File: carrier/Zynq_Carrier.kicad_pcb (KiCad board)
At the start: 4 copper layers, 148 x 137 mm, 533 parts, among them J11001 Header_2x20_2.54mm, J12001 HDMI-019S, J14001 HDMI-019S, J15001 AFC07-S40FCA-00, J16001 TF-01A, J17001 TYPE-C-31-M-12, J18001 DS1024-2x6R2, J18002 DS1024-2x6R2, J19001 DS1024-2x6R2, J2001 ZX-SH1.0-4PWT, J23001 KH-5224-8P8C-D, J24001 DF40C-100DS-0.4V(51), J25002 DF40C-100DS-0.4V(51), J26003 DF40C-100DS-0.4V(51), J29001 TYPE-C-31-M-12, J31001 TYPE-C-31-M-12, J32002 TYPE-C-31-M-12, J8001 SFW15R-1STE1LF, J9001 878311420, J9002 HX_JN1.27-2x5, Q20001 AO3400A, SW1001 DSHP04TSGER, SW19001 DSHP04TSGER, SW28001 DSHP04TSGER, SW33001 USER, SW33002 USER, SW33003 USER, SW33004 USER, SW7001 DSHP04TSGER, SW7002 DSHP08TSGER, SW7003 TS-1187A-B-A-B, SW7004 TS-1187A-B-A-B, SW7005 TS-1187A-B-A-B, SW7006 DSHP04TSGER, SW9001 DIP-4, SW9002 RESET, T10001 HX5008NLT, U1001 SY6280AAC, U1002 PCA9306DCUR, U11001 TLV75725PDYDR, U12001 M24C02-WMN6TP, U12002 TPD4E02B04DQAR, U12003 TPD4E02B04DQAR, U12004 TPD4E05U06DQAR, U14001 TPD12S016PWR, U15001 SY7201ABC, U15002 USBLC6-2SC6, U16001 TXS02612RTWR, U16002 TPD6E001RSER, U17001 TPS26631PWPR, U17002 USBLC6-2SC6, U19001 SY6280AAC, U19002 TPD4E1U06, U19003 TPD4E1U06, U20001 LM61460AANRJRR, U20002 LM61460AANRJRR, U20003 AP2112K-1.8, U2001 USBLC6-2SC6, U21001 INA3221AIRGVR, U21002 INA3221AIRGVR, U22004 LM61460AANRJRR, U27001 CP2102N-A02, U28001 CH347T, U28002 SN74LVC125ADR, U28004 AP2112K-3.3TRG1, U29001 USBLC6-2SC6, U30001 FUSB302BMPX, U3001 24AA025E48T-I/OT, U3002 RV-3028-C7-32.768kHz-1ppm-TA-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, U3003 TPS3823-33DBVR, U31001 USBLC6-2SC6, U32001 TPS2051CDBVR, U32002 USBLC6-2SC6, U4001 SN74LVC1G08, U4002 SN74LVC1G08, U4003 SN74LVC1G08, U5001 SN74LVC1G08, U5002 SN74LVC1G08, U5003 SN74LVC1G08, U5004 SN74LVC1G08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

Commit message: fix: USB-C mated INWARD — correct BOTH footprint mating-face AND 3D model + the gate
User caught (at an ANGLE — top-down hid it) that all 4 USB-C (J17001/J29001/J31001/
J32002) opened their cavity INBOARD. A full ultracode 2D-vs-3D angle audit of every
component confirmed the USB-C is the ONLY mismatch class; all other connectors +
components are correct. Two real defects, both fixed:

1. FOOTPRINT mating face: CONN_MATING_FACE["TYPE-C-31-M-12"] "-Y" -> "+Y". The 12 SMD
   signal contacts are the dense row at local -Y, so the mouth is OPPOSITE = +Y. With
   "-Y" the placer left the pads' mouth facing inboard on the N edge; "+Y" places the
   4 USB-C at rot 180 with the pad mouth toward the edge.
2. 3D MODEL: the EasyEDA .wrl was authored with its cavity 180 deg from its own
   footprint (cavity at the SMT-tail side). parts/TYPE-C-31-M-12/TYPE-C-31-M-12.kicad_mod
   model (rotate (xyz 0 0 0)) -> (xyz 0 0 180) aligns the model cavity with the
   footprint mouth; offset unchanged. ANGLED render confirms the cavity now faces
   off-board for all 4.

GATE fixes (LAW 4 — it MISSED this; make it correct, not softer):
 * connector_model_gate._tail_row_mouth: derive the tail row from EVERY pad (was
   _NUMERIC-only, which matched only the 4 shell legs and missed the 12 signal
   contacts named B8/A5/... — so it spuriously "agreed" with the wrong -Y). Now the
   densest y-row is the real contact row; mouth opposite -> correctly derives +Y.
 * bad-Z check: model rotate Z must be 0 OR 180 (axis-aligned; 180 = valid in-plane
   mouth flip for a .wrl authored on the opposite end). Was "0 mod 360" — a
   misdiagnosis that BOTH forbade the corrective 180 and gave false confidence to a
   .wrl mis-authored at 0. 90/270 (perpendicular) and non-orthogonal still fail.
   The model OPENING direction remains the render's job (LAW 5/6) — the gate can't render.

Verified: 148x137, DRC 0, all LAW-5/6 gates PASS (0 bad-Z, 0 geom-conflict), 3D MODELS
55/55, 633 tests pass, USB-C cavities rend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
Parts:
- moved J17001 0.25 mm to (91.8, 28.8), turned to 180 degrees
- moved J29001 0.25 mm to (129.9, 28.8), turned to 180 degrees
- moved J31001 0.25 mm to (141.4, 28.8), turned to 180 degrees
- moved J32002 0.25 mm to (114.7, 28.8), turned to 180 degrees

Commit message: feat: short FUNCTION descriptor on silk beside every off-board connector
User: "very short descriptors for each connector so we know which connector is for
what." Added a programmatic top-silk label per off-board connector, derived from its
subsystem sheet (never hand-placed):
  PWR (USB-C PD in) · USB OTG · JTAG · UART · microSD · HDMI TX · HDMI RX · ETH ·
  QWIIC · CAM · LCD · PMOD0/1/2
placed just inboard of the connector courtyard, centred on its along-edge axis.

The connector's J-ref is HIDDEN on silk (the function label owns the clear spot — the
ref was the space competitor; it stays in the footprint data for the netlist/BOM).
This is the dev-board idiom: label connectors by FUNCTION, not "J17001".

Implementation (schgen/generate/pcb.py): _CONN_DESC (sheet->label) + the PMODs
numbered in ref order; _connector_descriptors() emits the gr_text labels (F.SilkS,
size 1.1) and emit_pcb appends them; _embed_footprint hides the Reference property
for CONN_MATING_FACE parts. Verified silk-only AND 3D render per edge — all 14 labels
read cleanly, no overlap (the earlier "clutter" was the non-printed F.Fab layer).

Verified: 148x137, DRC 0, BOARD PASS, all gates green, 636 tests pass (+3 new
descriptor tests: all functions present, on-board F.SilkS, connector refs hidden /
IC refs kept).

Co-Authored-By: Claude Opus 4.8 <noreply@anthropic.com>
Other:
- board text added: "CAM"
- board text added: "ETH"
- board text added: "HDMI RX"
- board text added: "HDMI TX"
- board text added: "JTAG"
- board text added: "LCD"
- board text added: "PMOD0"
- board text added: "PMOD1"
- board text added: "PMOD2"
- board text added: "PWR"
- board text added: "QWIIC"
- board text added: "UART"
- board text added: "USB OTG"
- board text added: "microSD"
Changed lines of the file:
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@@
 			"Reference"
 			"J12001"
+			(hide yes)
 			(at 0 -5.42 0)
 			(layer "F.SilkS")
@@
 			"Reference"
 			"J14001"
+			(hide yes)
 			(at 0 -5.42 0)
 			(layer "F.SilkS")
@@
 			"Reference"
 			"J15001"
+			(hide yes)
 			(at 0 -3.44 0)
 			(layer "F.SilkS")
@@
 			"Reference"
 			"J16001"
+			(hide yes)
 			(at 0 -7.28 0)
 			(layer "F.SilkS")
@@
 			"Reference"
 			"J17001"
+			(hide yes)
 			(at 0 -4.47 0)
 			(layer "F.SilkS")
@@
 			"Reference"
 			"J18001"
+			(hide yes)
 			(at 0 -3.27 0)
 			(layer "F.SilkS")
@@
 			"Reference"
 			"J18002"
+			(hide yes)
 			(at 0 -3.27 0)
 			(layer "F.SilkS")
@@
 			"Reference"
 			"J19001"
+			(hide yes)
 			(at 0 -3.27 0)
 			(layer "F.SilkS")
@@
 			"Reference"
 			"J2001"
+			(hide yes)
 			(at 0 -3.7 0)
 			(layer "F.SilkS")
@@
 			"Reference"
 			"J23001"
+			(hide yes)
 			(at 0 -8.5 0)
 			(layer "F.SilkS")
@@
 			"Reference"
 			"J29001"
+			(hide yes)
 			(at 0 -4.47 0)
 			(layer "F.SilkS")
@@
 			"Reference"
 			"J31001"
+			(hide yes)
 			(at 0 -4.47 0)
 			(layer "F.SilkS")
@@
 			"Reference"
 			"J32002"
+			(hide yes)
 			(at 0 -4.47 0)
 			(layer "F.SilkS")
@@
 			"Reference"
 			"J8001"
+			(hide yes)
 			(at 0 -3.05 0)
 			(layer "F.SilkS")
@@
 			)
 		)
+	)
+	(gr_text
+		"HDMI RX"
+		(at 44.11 150.8 0)
+		(layer "F.SilkS")
+		(effects
+			(font
+				(size 1.1 1.1)
+				(thickness 0.2)
+			)
+		)
+	)
+	(gr_text
+		"HDMI TX"
+		(at 80.94 150.8 0)
+		(layer "F.SilkS")
+		(effects
+			(font
+				(size 1.1 1.1)
+				(thickness 0.2)
+			)
+		)
+	)
+	(gr_text
+		"LCD"
+		(at 32.336 100.98 0)
+		(layer "F.SilkS")
+		(effects
+			(font
+				(size 1.1 1.1)
+				(thickness 0.2)
+			)
+		)
+	)
+	(gr_text
+		"microSD"
+		(at 74.95 39.402 0)
+		(layer "F.SilkS")
+		(effects
+			(font
+				(size 1.1 1.1)
+				(thickness 0.2)
+			)
+		)
+	)
+	(gr_text
+		"PWR"
+		(at 91.835 33.698 0)
+		(layer "F.SilkS")
+		(effects
+			(font
+				(size 1.1 1.1)
+				(thickness 0.2)
+			)
+		)
+	)
+	(gr_text
+		"PMOD0"
+		(at 121.45 155.482 0)
+		(layer "F.SilkS")
+		(effects
+			(font
+				(size 1.1 1.1)
+				(thickness 0.2)
+			)
+		)
+	)
+	(gr_text
+		"PMOD1"
+		(at 138.19 155.482 0)
+		(layer "F.SilkS")
+		(effects
+			(font
+				(size 1.1 1.1)
+				(thickness 0.2)
+			)
+		)
+	)
+	(gr_text
+		"PMOD2"
+		(at 155.74 155.482 0)
+		(layer "F.SilkS")
+		(effects
+			(font
+				(size 1.1 1.1)
+				(thickness 0.2)
+			)
+		)
+	)
+	(gr_text
+		"QWIIC"
+		(at 165.3 100.27 0)
+		(layer "F.SilkS")
+		(effects
+			(font
+				(size 1.1 1.1)
+				(thickness 0.2)
+			)
+		)
+	)
+	(gr_text
+		"ETH"
+		(at 155.7 87.17 0)
+		(layer "F.SilkS")
+		(effects
+			(font
+				(size 1.1 1.1)
+				(thickness 0.2)
+			)
+		)
+	)
+	(gr_text
+		"JTAG"
+		(at 129.935 33.698 0)
+		(layer "F.SilkS")
+		(effects
+			(font
+				(size 1.1 1.1)
+				(thickness 0.2)
+			)
+		)
+	)
+	(gr_text
+		"UART"
+		(at 141.365 33.698 0)
+		(layer "F.SilkS")
+		(effects
+			(font
+				(size 1.1 1.1)
+				(thickness 0.2)
+			)
+		)
+	)
+	(gr_text
+		"USB OTG"
+		(at 114.695 33.698 0)
+		(layer "F.SilkS")
+		(effects
+			(font
+				(size 1.1 1.1)
+				(thickness 0.2)
+			)
+		)
+	)
+	(gr_text
+		"CAM"
+		(at 32.4 75.72 0)
+		(layer "F.SilkS")
+		(effects
+			(font
+				(size 1.1 1.1)
+				(thickness 0.2)
+			)
+		)

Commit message: feat: silk descriptors for the interior headers too (GPIO / JTAG / SWD)
Extend the self-documenting silk labels to the on-board developer headers (user:
"each connector"): J11001 -> GPIO (FMC-site 2x20 breakout), J9001 -> JTAG (Zynq 2x7
2.00mm header), J9002 -> SWD (system-controller ARM 10-pin). Labels placed below
each header; their J-refs hidden like the off-board connectors. The SoM DF40
mezzanines are intentionally NOT labelled — the "Zynq SoM" body silk already marks
that region (the module mounts on them).

_INT_DESC (ref->label) added at module level; _embed_footprint hides the ref for
CONN_MATING_FACE OR _INT_DESC; _connector_descriptors emits the interior labels.
Render-verified (silk-only): GPIO/JTAG/SWD readable beside their headers.

Verified: 148x137, DRC 0, BOARD PASS, all gates; descriptor tests updated
(GPIO/SWD present, interior count, J11001 ref hidden).

Co-Authored-By: Claude Opus 4.8 <noreply@anthropic.com>
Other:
- board text added: "GPIO"
- board text added: "SWD"
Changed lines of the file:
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@@
 			"Reference"
 			"J11001"
+			(hide yes)
 			(at 1.27 -2.38 0)
 			(layer "F.SilkS")
@@
 			"Reference"
 			"J9001"
+			(hide yes)
 			(at 0 -3 0)
 			(layer "F.SilkS")
@@
 			"Reference"
 			"J9002"
+			(hide yes)
 			(at 0 -4.02 0)
 			(layer "F.SilkS")
@@
 		(layer "F.SilkS")
 		(effects
+			(font
+				(size 1.1 1.1)
+				(thickness 0.2)
+			)
+		)
+	)
+	(gr_text
+		"GPIO"
+		(at 98.845 71.15 0)
+		(layer "F.SilkS")
+		(effects
+			(font
+				(size 1.1 1.1)
+				(thickness 0.2)
+			)
+		)
+	)
+	(gr_text
+		"JTAG"
+		(at 102.855 142.234 0)
+		(layer "F.SilkS")
+		(effects
+			(font
+				(size 1.1 1.1)
+				(thickness 0.2)
+			)
+		)
+	)
+	(gr_text
+		"SWD"
+		(at 100.88 135.434 0)
+		(layer "F.SilkS")
+		(effects

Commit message: fix: 3 CRITICAL electrical defects from the multi-agent audit (SW2 / LCD D1 / JTAG TDI-TDO)
A 69-agent electrical audit (35 per-subsystem + 7 cross-cutting, every finding
adversarially refuted) surfaced 3 board-dead CRITICAL defects that passed DRC/ERC/
netlist-equivalence. Each independently re-verified from the source artifacts before
fixing (per the "audits over-confirm; fixes can introduce bugs" rule):

1. SW2 (DSHP08) module DIP shorted all enables. Each DIP rocker bridges the two
   pads in the SAME COLUMN; the DSHP08 footprint numbers its bottom row 9..16
   (UNLIKE DSHP04's 8..5), so positions pair (n, n+8) — but the adapter re-used
   DSHP04's (n,17-n) diagonal, shorting +3V3_SC to itself on 1/3/5/7 and tying two
   enable nets on 2/4/6/8. All 7 module enables stuck off. FIX in the ADAPTER
   (+3V3_SC on top pins 1-8, BU_DIP nets on bottom pins 9-16) — NOT by renumbering
   the faithful EasyEDA footprint as the audit suggested (that would corrupt the
   real-part mapping; "never redraw parts"). DSHP08 is used only by SW2.
   + footprint-aware regression test (reads same-column pairs, asserts each rocker
     bridges +3V3_SC -> one unique BU_DIP enable) for SW2 and SW1.

2. LCD SY7201 boost catch diode D1 (SS34) reversed — cathode on LX, anode on the
   output, so the boost could never pump VLED+ (dead backlight). Device:D_Schottky
   is pin1=K/pin2=A; put K (D1.1) on the output, A (D1.2) on LX. The dossier was
   already correct; the netlist contradicted it.

3. usb_jtag CH347T TDI/TDO swapped — pin7=RTS0/MISO/TDO (bridge input), pin8=
   TXD0/MOSI/TDI (bridge output). DBG_FT_TDI sat on the input pin (buffer 2A had
   no driver) and DBG_FT_TDO on the output pin (collides with buffer 3Y when the
   bridge enables). Swapped to U1.8/U1.7; doc table corrected.

Verified: 148x137, DRC 0, netlist-equivalence PASS on all 35 sheets, every LAW gate
green, 68 subsystem tests pass.

Co-Authored-By: Claude Opus 4.8 <noreply@anthropic.com>
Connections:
- D15001 pad 1: Net-(D15001-K) -> /lcd/LCD_VLED_P
- D15001 pad 2: /lcd/LCD_VLED_P -> Net-(D15001-A)
- L15001 pad 2: Net-(D15001-K) -> Net-(D15001-A)
- SW7002 pad 10: BU_DIP_PMOD -> BU_DIP_HDMI_RX
- SW7002 pad 11: +3V3_SC -> BU_DIP_LCD
- SW7002 pad 12: BU_DIP_SD -> BU_DIP_CAM
- SW7002 pad 13: +3V3_SC -> BU_DIP_SD
- SW7002 pad 14: BU_DIP_LCD -> BU_DIP_USB
- SW7002 pad 15: +3V3_SC -> BU_DIP_PMOD
- SW7002 pad 16: BU_DIP_HDMI_TX -> BU_DIP_SPARE
- SW7002 pad 2: BU_DIP_HDMI_RX -> +3V3_SC
- SW7002 pad 4: BU_DIP_CAM -> +3V3_SC
- SW7002 pad 6: BU_DIP_USB -> +3V3_SC
- SW7002 pad 8: BU_DIP_SPARE -> +3V3_SC
- SW7002 pad 9: +3V3_SC -> BU_DIP_HDMI_TX
- U15001 pad 1: Net-(D15001-K) -> Net-(D15001-A)
- U28001 pad 7: /usb_jtag/DBG_FT_TDI -> /usb_jtag/DBG_FT_TDO
- U28001 pad 8: /usb_jtag/DBG_FT_TDO -> /usb_jtag/DBG_FT_TDI
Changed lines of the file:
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@@
 	(net 271 "Net-(C22021-Pad2)")
 	(net 272 "Net-(D1001-K)")
-	(net 273 "Net-(D15001-K)")
+	(net 273 "Net-(D15001-A)")
 	(net 274 "Net-(D19001-K)")
 	(net 275 "Net-(D20001-K)")
@@
 			(layers "F.Cu" "F.Mask" "F.Paste")
 			(roundrect_rratio 0.138889)
-			(net 273 "Net-(D15001-K)")
+			(net 47 "/lcd/LCD_VLED_P")
 		)
 		(pad
@@
 			(layers "F.Cu" "F.Mask" "F.Paste")
 			(roundrect_rratio 0.138889)
-			(net 47 "/lcd/LCD_VLED_P")
+			(net 273 "Net-(D15001-A)")
 		)
 		(embedded_fonts no)
@@
 			(size 1.599997 3.499993)
 			(layers "F.Cu" "F.Paste" "F.Mask")
-			(net 273 "Net-(D15001-K)")
+			(net 273 "Net-(D15001-A)")
 		)
 		(pad
@@
 			(size 0.759993 1.599997)
 			(layers "F.Cu" "F.Paste" "F.Mask")
-			(net 84 "BU_DIP_HDMI_RX")
+			(net 14 "+3V3_SC")
 		)
 		(pad
@@
 			(size 0.759993 1.599997)
 			(layers "F.Cu" "F.Paste" "F.Mask")
-			(net 83 "BU_DIP_CAM")
+			(net 14 "+3V3_SC")
 		)
 		(pad
@@
 			(size 0.759993 1.599997)
 			(layers "F.Cu" "F.Paste" "F.Mask")
-			(net 92 "BU_DIP_USB")
+			(net 14 "+3V3_SC")
 		)
 		(pad
@@
 			(size 0.759993 1.599997)
 			(layers "F.Cu" "F.Paste" "F.Mask")
-			(net 91 "BU_DIP_SPARE")
+			(net 14 "+3V3_SC")
 		)
 		(pad
@@
 			(size 0.759993 1.599997)
 			(layers "F.Cu" "F.Paste" "F.Mask")
-			(net 14 "+3V3_SC")
+			(net 85 "BU_DIP_HDMI_TX")
 		)
 		(pad
@@
 			(size 0.759993 1.599997)
 			(layers "F.Cu" "F.Paste" "F.Mask")
-			(net 89 "BU_DIP_PMOD")
+			(net 84 "BU_DIP_HDMI_RX")
 		)
 		(pad
@@
 			(size 0.759993 1.599997)
 			(layers "F.Cu" "F.Paste" "F.Mask")
-			(net 14 "+3V3_SC")
+			(net 87 "BU_DIP_LCD")
 		)
 		(pad
@@
 			(size 0.759993 1.599997)
 			(layers "F.Cu" "F.Paste" "F.Mask")
-			(net 90 "BU_DIP_SD")
+			(net 83 "BU_DIP_CAM")
 		)
 		(pad
@@
 			(size 0.759993 1.599997)
 			(layers "F.Cu" "F.Paste" "F.Mask")
-			(net 14 "+3V3_SC")
+			(net 90 "BU_DIP_SD")
 		)
 		(pad
@@
 			(size 0.759993 1.599997)
 			(layers "F.Cu" "F.Paste" "F.Mask")
-			(net 87 "BU_DIP_LCD")
+			(net 92 "BU_DIP_USB")
 		)
 		(pad
@@
 			(size 0.759993 1.599997)
 			(layers "F.Cu" "F.Paste" "F.Mask")
-			(net 14 "+3V3_SC")
+			(net 89 "BU_DIP_PMOD")
 		)
 		(pad
@@
 			(size 0.759993 1.599997)
 			(layers "F.Cu" "F.Paste" "F.Mask")
-			(net 85 "BU_DIP_HDMI_TX")
+			(net 91 "BU_DIP_SPARE")
 		)
 		(model
@@
 			(size 1.099998 0.599999)
 			(layers "F.Cu" "F.Paste" "F.Mask")
-			(net 273 "Net-(D15001-K)")
+			(net 273 "Net-(D15001-A)")
 		)
 		(pad
@@
 			(size 0.364007 1.742008)
 			(layers "F.Cu" "F.Paste" "F.Mask")
-			(net 66 "/usb_jtag/DBG_FT_TDI")
+			(net 67 "/usb_jtag/DBG_FT_TDO")
 		)
 		(pad
@@
 			(size 0.364007 1.742008)
 			(layers "F.Cu" "F.Paste" "F.Mask")
-			(net 67 "/usb_jtag/DBG_FT_TDO")
+			(net 66 "/usb_jtag/DBG_FT_TDI")
 		)
 		(pad

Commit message: fix(audit MEDIUM): ESD-clamp the two plain Pmod host ports (16 bank-13 IO)
Audit finding: pmod.py's two Digilent host ports exposed 16 Zynq bank-13 GPIO
off-board through only a 200R series resistor, while every other external
connector (and the sibling pmod_expansion) carries a low-cap TVS — a self-
inconsistent protection policy. Add a TPD4E1U06 (0.8pF, C124691) GND-referenced
shunt clamp per IO: two 4-channel arrays per port (U1..U4).

Placement-engine note: clamping the SOCKET-side net (as pmod_expansion does)
meshes the float-net lineariser through the shared 4-channel array because pmod
ALSO has the 200R series (pmod_expansion does not), tripping
"single-ended chain without a rail/GND end". Resolved by clamping the SoM-side
(FPGA-pin) net just inboard of the 200R instead: series-R + shunt-TVS at the
protected pin is a standard IC-ESD topology that directly clamps the bank-13 IO,
and it keeps each socket leg the exact 2-pin chain the working baseline had.

+ regression test: all 16 host-signal nets reach an array channel, arrays
grounded on pin 2, pin 5 the only intentional NC. Verified: 148x137, DRC 0,
BOARD PASS, all gates; pmod test 23/23.

Co-Authored-By: Claude Opus 4.8 <noreply@anthropic.com>
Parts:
- added U18001: TPD4E1U06, TPD4E1U06DBVR:TPD4E1U06DBVR, F.Cu at (115.5, 142.1)
- added U18002: TPD4E1U06, TPD4E1U06DBVR:TPD4E1U06DBVR, F.Cu at (120.6, 142.1)
- added U18003: TPD4E1U06, TPD4E1U06DBVR:TPD4E1U06DBVR, F.Cu at (125.6, 142.1)
- added U18004: TPD4E1U06, TPD4E1U06DBVR:TPD4E1U06DBVR, F.Cu at (130.7, 142.1)

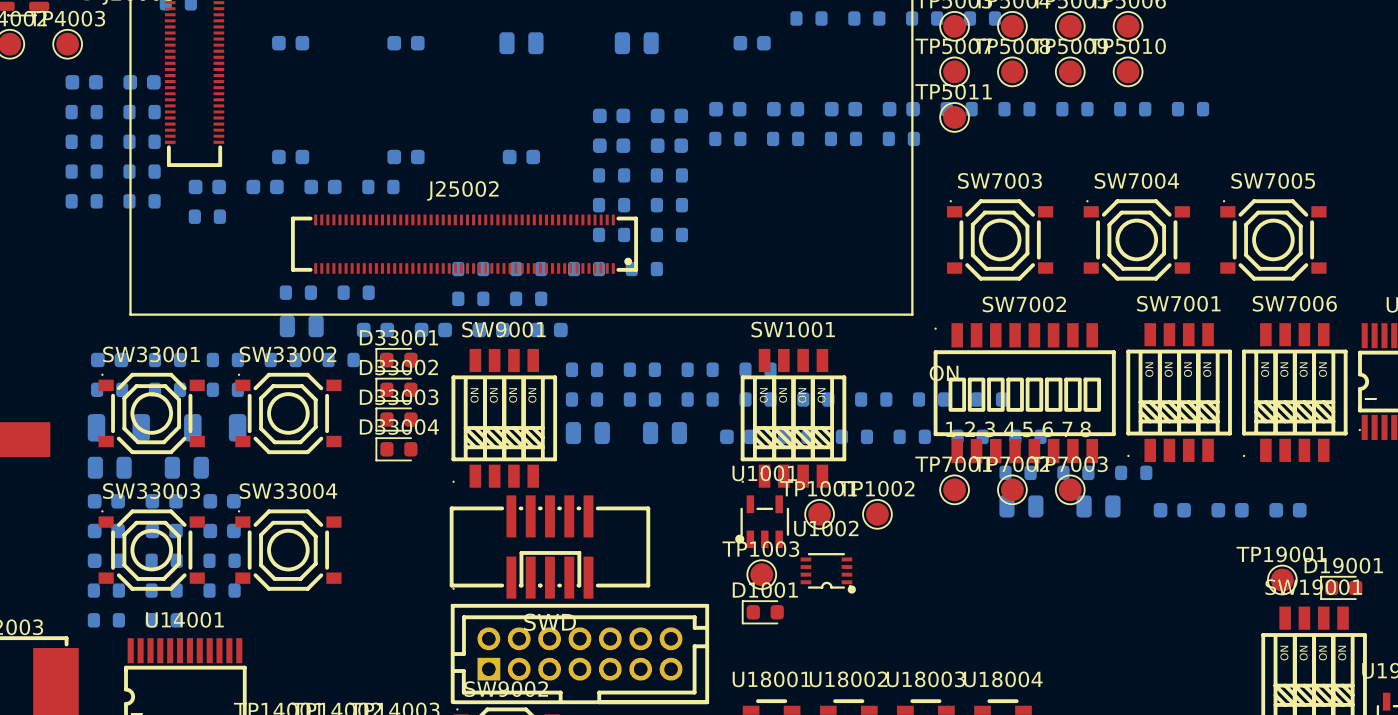
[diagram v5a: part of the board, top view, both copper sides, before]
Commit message: fix(audit LOW): board_aux rail bulk cap + ethernet CT engineering-decision doc
- board_aux (implement): add a 10uF/25V (C15850) bulk hold-up cap on the gated
  +3V3_AUX rail at the SY6280 output — only a 100n was present and the DS
  recommends an output cap for the 200mA QWIIC load. Additive shunt (LAW-0 safe);
  .py + .cir + header updated; soft-start tolerates it. 538 footprints, BOARD PASS.
- ethernet CT (documented decision, not blind-implemented): the four chip-side
  magnetics centre taps stay open — the RTL8211F voltage-mode PHY self-biases
  (COMPLIANCE ETH-5 PASS). Realtek's CT->GND EMI cap is recorded as a DEFERRED
  EMC-tuning provision: this reusable magnetics library exposes only CHASSIS_GND
  (no signal GND), and CT-cap values are tuned against measured emissions — add at
  the EMC bring-up revision, not as a blind value in the library.

Verified: 148x137, DRC 0, BOARD PASS; board_aux + ethernet tests 34/34.

Co-Authored-By: Claude Opus 4.8 <noreply@anthropic.com>
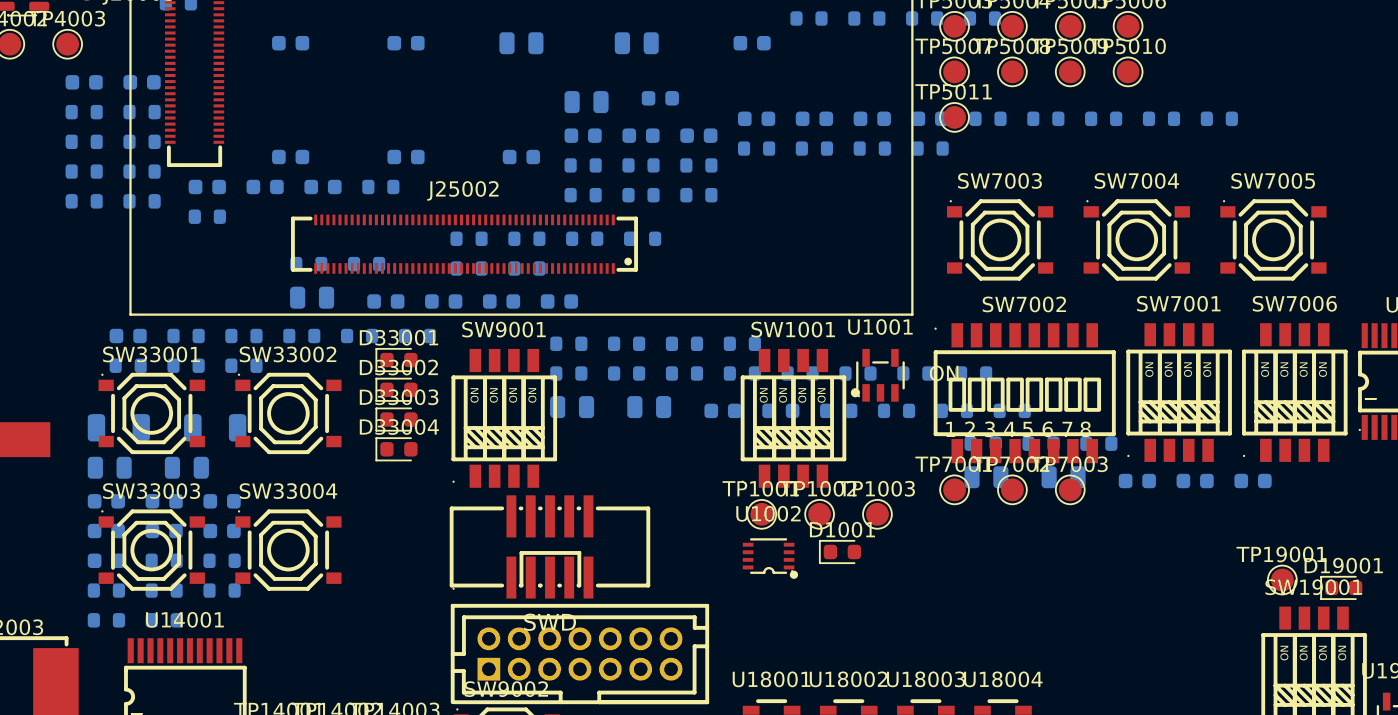
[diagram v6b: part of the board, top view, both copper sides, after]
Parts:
- added C1005: 100n, Capacitor_SMD:C_0603_1608Metric, B.Cu at (110.7, 103.3)
- C1003: value 100n -> 10u; footprint Capacitor_SMD:C_0603_1608Metric -> Capacitor_SMD:C_0805_2012Metric
- moved U1001 12.3 mm to (122.7, 119.1)
- moved TP1003 8.59 mm to (122.5, 128.3)
- moved D1001 6.45 mm to (120.1, 130.8)
- moved R1003 6.32 mm to (110.7, 105.3)
- moved C1002 5.83 mm to (103.1, 103.3)
- moved R1004 5.72 mm to (103.1, 107.3)
- moved U1002 3.93 mm to (115.3, 131.0)
- moved TP1001 3.81 mm to (114.8, 128.3)
- moved TP1002 3.81 mm to (118.6, 128.3)
- moved C1001 3.41 mm to (108.1, 100.9)
- moved C1003 3.31 mm to (103.3, 101.1)
- moved R1005 3.26 mm to (106.9, 107.3)
- moved R1006 3.26 mm to (110.7, 107.3)
- moved C19001 3.00 mm to (139.6, 126.1)
- moved C19002 3.00 mm to (129.6, 125.8)
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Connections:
- C1003 pad 1: +3V3_SC -> +3V3_AUX
- C1004 pad 1: +3V3_AUX -> +3V3_SC
